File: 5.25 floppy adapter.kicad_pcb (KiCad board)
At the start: 2 copper layers, 44.2 x 21.3 mm, 2 parts

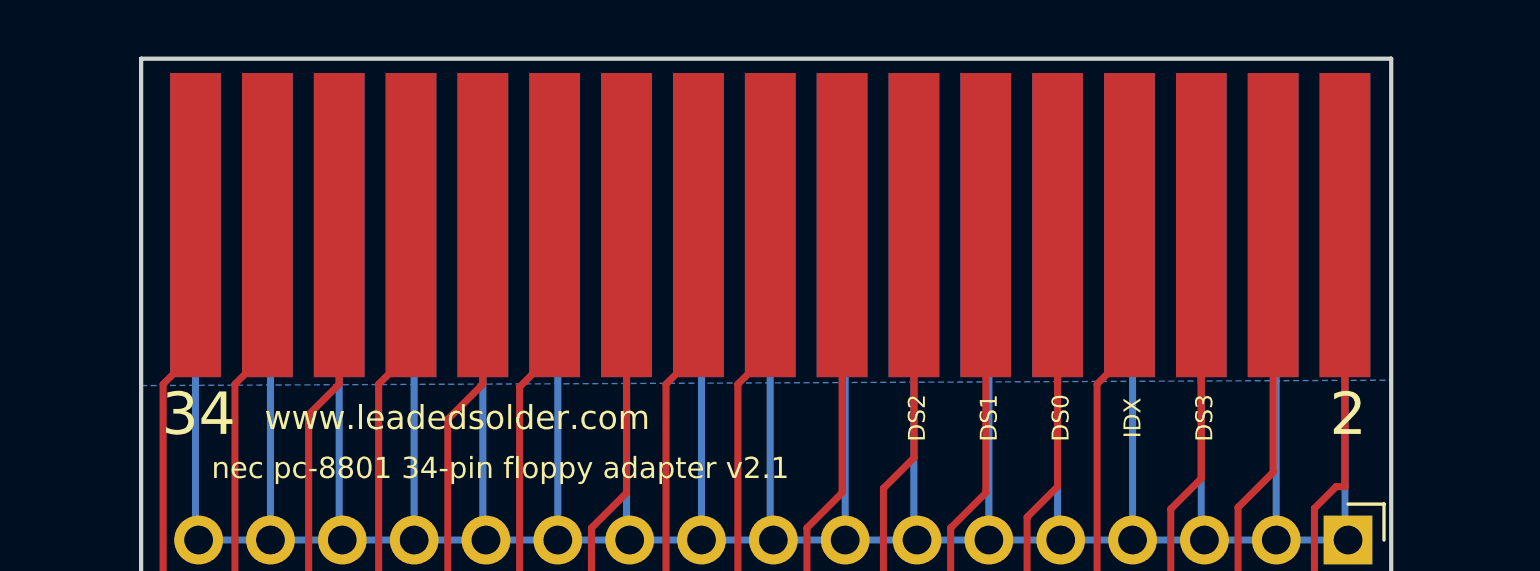
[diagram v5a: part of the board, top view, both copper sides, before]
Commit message: 1.21mm backed to allow for bevel
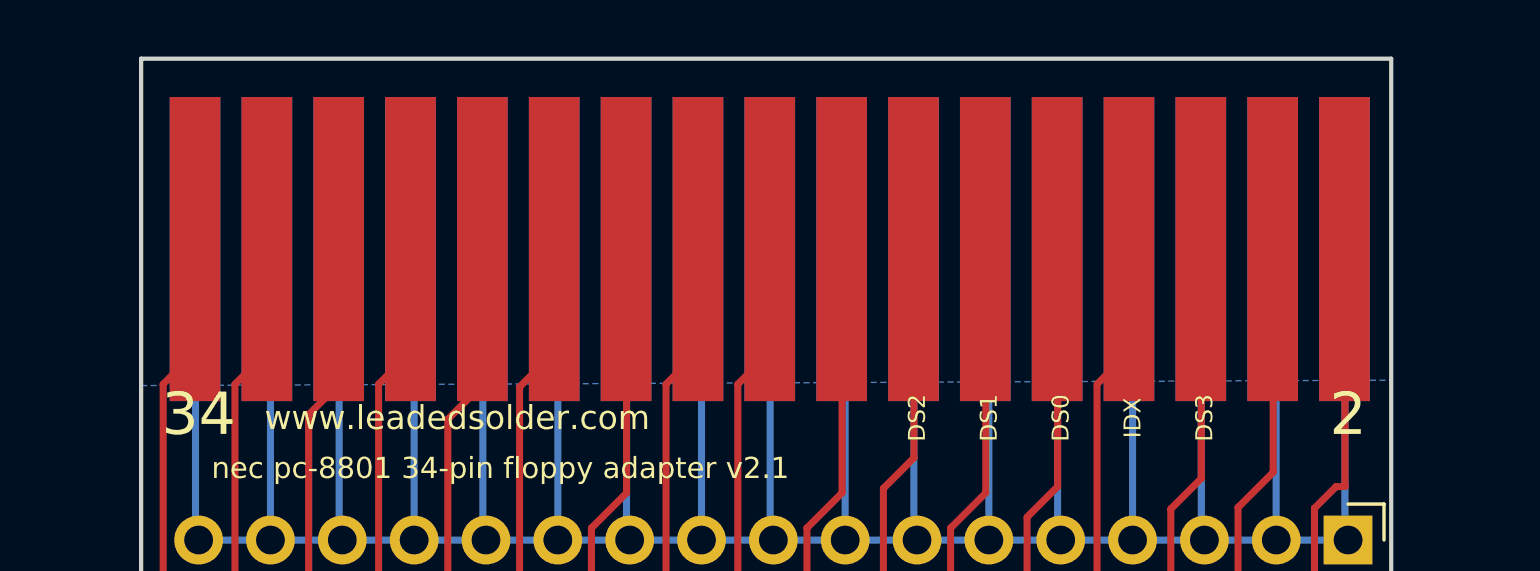
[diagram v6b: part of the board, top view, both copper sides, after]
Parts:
- moved N1 0.85 mm to (177.7, 87.5)
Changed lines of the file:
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@@
   )
   (module FloppyBits:525_male_edge (layer F.Cu)
-    (at 177.69 86.655)
+    (at 177.673 87.503)
     (tags floppy)
     (attr smd)

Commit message: Move labels
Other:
- board text added: "edge-connector floppy adapter v2.1"
- board text added: "www.leadedsolder.com 2020"
- board text removed: "nec pc-8801 34-pin floppy adapter v2.1"
- board text removed: "www.leadedsolder.com"
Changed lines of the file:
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@@
       (net 13 GND) (clearance 0.375))
   )
-  (gr_text DS2 (at 182.88 90.932 90) (layer F.SilkS)
+  (gr_text DS2 (at 182.88 91.3765 90) (layer F.SilkS)
     (effects (font (size 0.6 0.6) (thickness 0.15)))
   )
-  (gr_text DS1 (at 185.42 90.932 90) (layer F.SilkS)
+  (gr_text DS1 (at 185.42 91.3765 90) (layer F.SilkS)
     (effects (font (size 0.6 0.6) (thickness 0.15)))
   )
-  (gr_text DS0 (at 187.96 90.932 90) (layer F.SilkS)
+  (gr_text DS0 (at 187.96 91.3765 90) (layer F.SilkS)
     (effects (font (size 0.6 0.6) (thickness 0.15)))
   )
-  (gr_text IDX (at 190.5 90.932 90) (layer F.SilkS)
+  (gr_text IDX (at 190.4365 91.5035 90) (layer F.SilkS)
     (effects (font (size 0.6 0.6) (thickness 0.15)))
   )
-  (gr_text DS3 (at 193.04 90.932 90) (layer F.SilkS)
+  (gr_text DS3 (at 193.04 91.6305 90) (layer F.SilkS)
     (effects (font (size 0.6 0.6) (thickness 0.15)))
   )
@@
   (gr_line (start 199.644 99.568) (end 155.448 99.568) (layer Edge.Cuts) (width 0.15))
   (gr_line (start 199.644 78.232) (end 155.448 78.232) (layer Edge.Cuts) (width 0.15))
-  (gr_text 33 (at 157.48 90.805) (layer B.SilkS)
+  (gr_text 33 (at 157.48 91.7575) (layer B.SilkS)
     (effects (font (size 1.5 1.5) (thickness 0.3)) (justify mirror))
   )
-  (gr_text 1 (at 198.12 90.805) (layer B.SilkS)
+  (gr_text 1 (at 198.12 91.6305) (layer B.SilkS)
     (effects (font (size 1.5 1.5) (thickness 0.3)) (justify mirror))
   )
-  (gr_text 34 (at 157.48 90.805) (layer F.SilkS)
+  (gr_text 34 (at 157.48 91.7575) (layer F.SilkS)
     (effects (font (size 1.5 1.5) (thickness 0.3)))
   )
-  (gr_text 2 (at 198.12 90.805) (layer F.SilkS)
+  (gr_text 2 (at 198.12 91.6305) (layer F.SilkS)
     (effects (font (size 1.5 1.5) (thickness 0.3)))
   )
-  (gr_text www.leadedsolder.com (at 166.624 90.932) (layer F.SilkS)
+  (gr_text "www.leadedsolder.com 2020" (at 169.4815 91.44) (layer F.SilkS)
     (effects (font (size 0.85 0.85) (thickness 0.2125)))
   )
-  (gr_text "nec pc-8801 34-pin floppy adapter v2.1" (at 168.148 92.71) (layer F.SilkS)
+  (gr_text "edge-connector floppy adapter v2.1" (at 170.942 92.71) (layer F.SilkS)
     (effects (font (size 0.75 0.75) (thickness 0.1875)))
   )

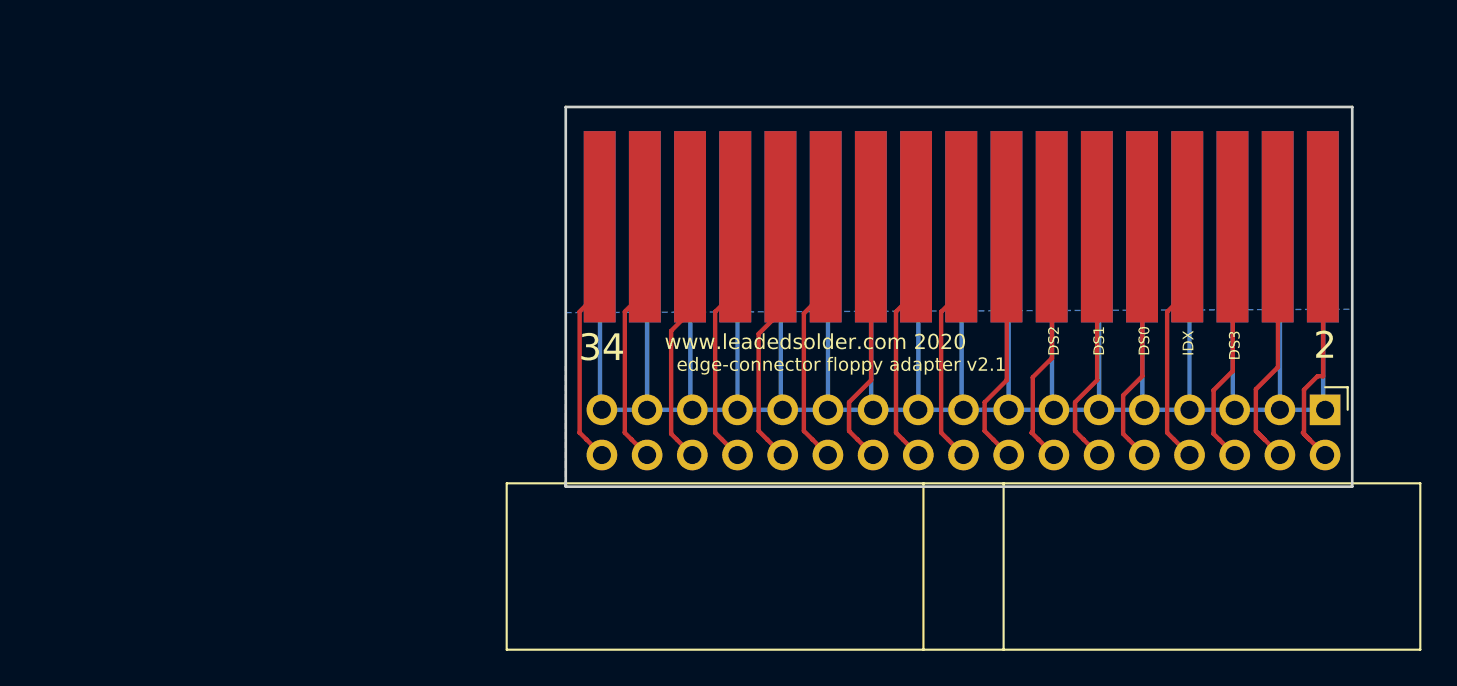
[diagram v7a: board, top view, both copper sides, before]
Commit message: Add a chamfer
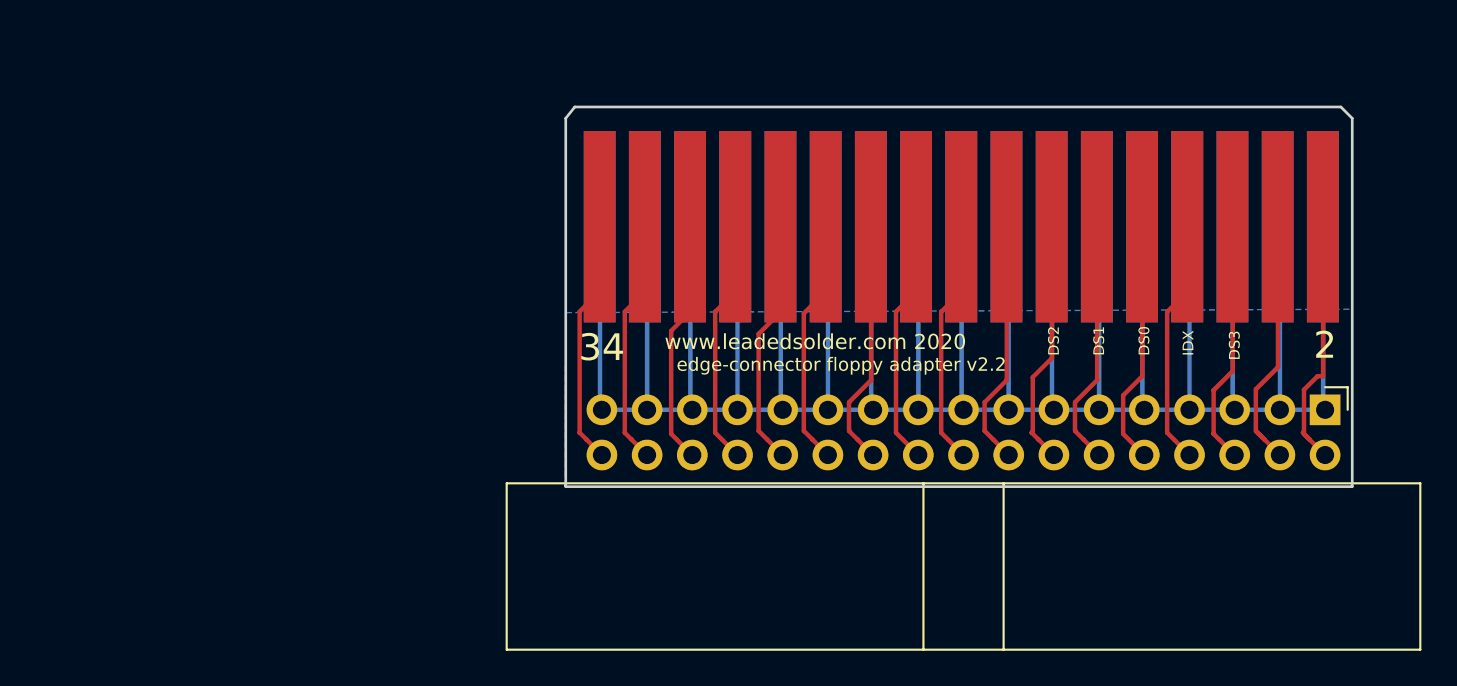
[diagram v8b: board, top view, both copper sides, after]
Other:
- outline, holes or cut-outs redrawn
- board text added: "edge-connector floppy adapter v2.2"
- board text removed: "edge-connector floppy adapter v2.1"
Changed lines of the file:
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@@
   (general
     (thickness 1.6)
-    (drawings 15)
+    (drawings 17)
     (tracks 128)
     (zones 0)
@@
       (net 13 GND) (clearance 0.375))
   )
+  (gr_line (start 155.956 78.232) (end 199.009 78.232) (layer Edge.Cuts) (width 0.15))
+  (gr_line (start 155.448 78.867) (end 155.956 78.232) (layer Edge.Cuts) (width 0.15))
+  (gr_line (start 199.644 78.867) (end 199.009 78.232) (layer Edge.Cuts) (width 0.15))
+  (gr_line (start 155.448 78.867) (end 155.448 99.568) (layer Edge.Cuts) (width 0.15))
+  (gr_line (start 199.644 78.867) (end 199.644 99.568) (layer Edge.Cuts) (width 0.15))
   (gr_text DS2 (at 182.88 91.3765 90) (layer F.SilkS)
     (effects (font (size 0.6 0.6) (thickness 0.15)))
@@
     (effects (font (size 0.6 0.6) (thickness 0.15)))
   )
-  (gr_line (start 155.448 99.568) (end 155.448 78.232) (layer Edge.Cuts) (width 0.15))
-  (gr_line (start 199.644 78.232) (end 199.644 99.568) (layer Edge.Cuts) (width 0.15))
   (gr_line (start 199.644 99.568) (end 155.448 99.568) (layer Edge.Cuts) (width 0.15))
-  (gr_line (start 199.644 78.232) (end 155.448 78.232) (layer Edge.Cuts) (width 0.15))
   (gr_text 33 (at 157.48 91.7575) (layer B.SilkS)
     (effects (font (size 1.5 1.5) (thickness 0.3)) (justify mirror))
@@
     (effects (font (size 0.85 0.85) (thickness 0.2125)))
   )
-  (gr_text "edge-connector floppy adapter v2.1" (at 170.942 92.71) (layer F.SilkS)
+  (gr_text "edge-connector floppy adapter v2.2" (at 170.942 92.71) (layer F.SilkS)
     (effects (font (size 0.75 0.75) (thickness 0.1875)))
   )
